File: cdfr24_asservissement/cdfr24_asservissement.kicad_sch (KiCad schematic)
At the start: 0 parts

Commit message: First draft of schematic
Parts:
- added C10: 4.7uF, Capacitor_SMD:C_0805_2012Metric_Pad1.18x1.45mm_HandSolder, symbol Device:C
- added C11: 100uF, Capacitor_SMD:CP_Elec_10x10.5, symbol Device:C_Polarized
- added C14, C15: 10pF, Capacitor_SMD:C_0805_2012Metric_Pad1.18x1.45mm_HandSolder, symbol Device:C
- added C25: 10nF, Capacitor_SMD:C_0805_2012Metric_Pad1.18x1.45mm_HandSolder, symbol Device:C
- added C26: 1uF, Capacitor_SMD:C_0805_2012Metric_Pad1.18x1.45mm_HandSolder, symbol Device:C
- added C27, C28, C29, C30, C32 (x3): 100nF, Capacitor_SMD:C_0805_2012Metric_Pad1.18x1.45mm_HandSolder, symbol Device:C
- added C33: 220uF, Capacitor_SMD:CP_Elec_10x10.5, symbol Device:C_Polarized
- added C7, C8: 470uF, Capacitor_SMD:CP_Elec_10x10.5, symbol Device:C_Polarized
- added D1, D2, D3, D4: LED, LED_SMD:LED_0805_2012Metric_Pad1.15x1.40mm_HandSolder, symbol Device:LED
- added D5: D_Zener, Diode_SMD:D_SOD-123, symbol Device:D_Zener
- added D6: DIODE, B170B:DIOM505270X240, symbol pspice:DIODE
- added J1: Connecteur batterie, TerminalBlockBend:CUI_TBP01R1-508-02BE, symbol Connector:Screw_Terminal_01x02
- added J10: Free Connecteur, Connector_PinHeader_2.54mm:PinHeader_1x08_P2.54mm_Vertical, symbol Connector:Conn_01x08_Male
- added J11, J12: Conn_01x02, Connector_JST:JST_XH_B2B-XH-A_1x02_P2.50mm_Vertical, symbol Connector_Generic:Conn_01x02
- added J13, J6: Connecteur Odométrie, Connector_JST:JST_XH_B4B-XH-A_1x04_P2.50mm_Vertical, symbol Connector_Generic:Conn_01x04
- added J2 (x2): Conn_01x03, TerminalBlockBend:CUI_TBP02R1-381-03BE, symbol Connector_Generic:Conn_01x03
- added J3 (x2): Conn_01x05, Connector_JST:JST_XH_B5B-XH-A_1x05_P2.50mm_Vertical, symbol Connector_Generic:Conn_01x05
- added J4: Connecteur Programmation, Connector_PinHeader_2.54mm:PinHeader_1x04_P2.54mm_Vertical, symbol Connector_Generic:Conn_01x04
- added J5: Conn_01x03, Connector_PinHeader_2.54mm:PinHeader_1x03_P2.54mm_Vertical, symbol Connector_Generic:Conn_01x03
- added J7: Conn_01x03, Connector_JST:JST_XH_B3B-XH-A_1x03_P2.50mm_Vertical, symbol Connector_Generic:Conn_01x03
- added JP1: Jumper_3_Open, Connector_PinHeader_2.54mm:PinHeader_1x03_P2.54mm_Vertical, symbol Jumper:Jumper_3_Open
- added L2: 10uH, IHLP2525CZER100M01:IND_IHLP_2525_CZ-M, symbol Device:L
- added Q13: Q_NMOS_GDS, Package_TO_SOT_SMD:TO-252-2, symbol Device:Q_NMOS_GDS
- added R1, R10, R19, R21, R44, R8: 10k, Resistor_SMD:R_0805_2012Metric_Pad1.20x1.40mm_HandSolder, symbol Device:R
- added R2: 2k4, Resistor_SMD:R_0805_2012Metric_Pad1.20x1.40mm_HandSolder, symbol Device:R
- added R20, R22, R9: 220, Resistor_SMD:R_0805_2012Metric_Pad1.20x1.40mm_HandSolder, symbol Device:R
- added R3: 150, Resistor_SMD:R_0805_2012Metric_Pad1.20x1.40mm_HandSolder, symbol Device:R
- added R4: 3k9, Resistor_SMD:R_0805_2012Metric_Pad1.20x1.40mm_HandSolder, symbol Device:R
- added R42, R43 (x3): 56k, Resistor_SMD:R_0805_2012Metric_Pad1.20x1.40mm_HandSolder, symbol Device:R
- added U1: LM317_SOT-223, Package_TO_SOT_SMD:SOT-223-3_TabPin2, symbol Regulator_Linear:LM317_SOT-223
- added U3: STM32F401RCTx, Package_QFP:LQFP-64_10x10mm_P0.5mm, symbol MCU_ST_STM32F4:STM32F401RCTx
- added U4: LSM6DSL, Package_LGA:LGA-14_3x2.5mm_P0.5mm_LayoutBorder3x4y, symbol Sensor_Motion:LSM6DSL
- added U4: LMR16020PDDA, Package_SO:SOIC-8-1EP_3.9x4.9mm_P1.27mm_EP2.41x3.3mm, symbol LMR16020PDDA:LMR16020PDDA
- added Y1: Crystal_GND24, Crystal:Crystal_SMD_2520-4Pin_2.5x2.0mm, symbol Device:Crystal_GND24
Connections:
- new net: JP1.2 (C), R21.1
- new net: J13.3 (Pin_3), U3.27 (PB1)
- new net: C14.2, R1.1, Y1.3
- new net: R1.2, U3.5 (PH0)
- new net: D4.1 (K), R22.1
- new net: J6.2 (Pin_2), U3.56 (PB4)
- new net: J6.3 (Pin_3), U3.57 (PB5)
- new net: D4.2 (A), U3.50 (PA15)
- new net: C32.2, D6.2 (A), L2.1, U4.8 (SW)
- new net: D5.1 (K), Q13.1 (G), R42.2
- new net: C15.1, R8.1, Y1.1
- new net: R8.2, U3.6 (PH1)
- new net: C32.1, U4.1 (BOOT)
- new net: D3.1 (K), R20.1
- new net: D3.2 (A), U3.45 (PA12)
- new net: J1.2 (Pin_2), Q13.2 (D)
- new net: R2.2, R4.1, U1.1 (ADJ)
- new net: R43.2, R44.1, U4.5 (FB)
- new net: J12.2 (Pin_2), R19.2, U3.52 (PC11)
- new net: D2.1 (K), R9.1
- new net: R21.2, U3.60 (BOOT0)
- new net: C10.1, U3.30 (VCAP1)
- new net: J11.2 (Pin_2), R10.2, U3.53 (PC12)
- new net: J4.4 (Pin_4), U3.7 (NRST)
- new net: D1.1 (K), R3.1
- new net +3.3V: C11.1, C25.1, C26.1, C27.1, C28.1, C29.1, C30.1, C32.1, C32.2, D1.2 (A), J11.1 (Pin_1), J12.1 (Pin_1), JP1.3 (B), R2.1, R43.1, R43.1, U1.2 (VO), U3.1 (VBAT), U3.13 (VREF+), U3.19 (VDD), U3.32 (VDD), U3.48 (VDD), U3.64 (VDD), U4.12 (CS), U4.5 (VDDIO), U4.8 (VDD)
- new net +5V: C33.1, D2.2 (A), J13.4 (Pin_4), J3.1 (Pin_1), J3.1 (Pin_1), J6.4 (Pin_4), L2.2, R43.1, U1.3 (VI)
- new net +BATT: C7.1, C8.1, J1.1 (Pin_1), R42.1, U4.2 (VIN), U4.3 (EN)
- new net BRAKE_L: U3.22 (PA6)
- new net BRAKE_R: U3.36 (PB15)
- new net EN_L: U3.23 (PA7)
- new net EN_R: U3.38 (PC7)
- new net FWD_L: U3.26 (PB0)
- new net FWD_R: U3.34 (PB13)
- new net Free1: J10.1 (Pin_1), U3.62 (PB9)
- new net Free2: J10.2 (Pin_2), U3.2 (PC13)
- new net Free3: J10.3 (Pin_3), U3.3 (PC14)
- new net Free4: J10.4 (Pin_4), U3.4 (PC15)
- new net Free5: J10.5 (Pin_5), U3.8 (PC0)
- new net Free6: J10.6 (Pin_6), U3.9 (PC1)
- new net Free7: J10.7 (Pin_7), U3.10 (PC2)
- new net Free8: J10.8 (Pin_8), U3.11 (PC3)
- new net GND: C10.2, C11.2, C14.1, C15.2, C25.2, C26.2, C27.2, C28.2, C29.2, C30.2, C32.1, C32.2, C33.2, C7.2, C8.2, D5.2 (A), D6.1 (K), J13.1 (Pin_1), J3.5 (Pin_5), J3.5 (Pin_5), J4.1 (Pin_1), J5.3 (Pin_3), J6.1 (Pin_1), J7.3 (Pin_3), JP1.1 (A), Q13.3 (S), R10.1, R19.1, R20.2, R22.2, R3.2, R4.2, R44.2, R9.2, U3.12 (VSSA), U3.18 (VSS), U3.31 (VSS), U3.47 (VSS), U3.63 (VSS), U4.1 (SDO/SA0), U4.2 (SDX), U4.3 (SCX), U4.4 (RT/SYNC), U4.6 (GND), U4.7 (GND), U4.7 (GND), U4.9 (THERMAL_PAD), Y1.2, Y1.4
- new net I2C_CLK: J7.1 (Pin_1), U3.58 (PB6)
- new net I2C_SDA: J7.2 (Pin_2), U3.59 (PB7)
- new net IMU_INT1: U3.41 (PA8), U4.4 (INT1)
- new net IMU_INT2: U3.42 (PA9), U4.9 (INT2)
- new net IMU_SCL: R43.2, U3.29 (PB10), U4.13 (SCL)
- new net IMU_SDA: R43.2, U3.55 (PB3), U4.14 (SDA)
- new net RX: J5.2 (Pin_2), U3.17 (PA3)
- new net SWCLK: J4.2 (Pin_2), U3.49 (PA14)
- new net SWDIO: J4.3 (Pin_3), U3.46 (PA13)
- new net TACHO_L: U3.21 (PA5)
- new net TACHO_R: U3.37 (PC6)
- new net TX: J5.1 (Pin_1), U3.16 (PA2)
- new net left_driver/H1: J3.4 (Pin_4)
- new net left_driver/H2: J3.3 (Pin_3)
- new net left_driver/H3: J3.2 (Pin_2)
- new net left_driver/OUT1: J2.3 (Pin_3)
- new net left_driver/OUT2: J2.2 (Pin_2)
- new net left_driver/OUT3: J2.1 (Pin_1)
- new net odometrie2: J13.2 (Pin_2), U3.54 (PD2)
- new net right_driver/H1: J3.4 (Pin_4)
- new net right_driver/H2: J3.3 (Pin_3)
- new net right_driver/H3: J3.2 (Pin_2)
- new net right_driver/OUT1: J2.3 (Pin_3)
- new net right_driver/OUT2: J2.2 (Pin_2)
- new net right_driver/OUT3: J2.1 (Pin_1)
- no-connect marks 0 -> 15
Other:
- added sheet left_driver (motor_driver.kicad_sch)
- added sheet right_driver (motor_driver.kicad_sch)
- note added: "3,6 v max pour VBATT (alim pour quartz) et 4 pour VDD"
- note added: "A verifier pour 2024 Speed_controle_1 : TIM1_CH2N Speed_controle_2 : TIM1_CH1N Info_vitesse_1 : TIM2 Info_vitesse_2 : TM3 Info_Courant_1 : ADC_IN1 Info_Courant_2 : ADC_IN11"
- note added: "Alimentation"
- note added: "I2C address 1101010b"
- note added: "I2C mode enabled"
- note added: "Speed control pin"
- note added: "TODO: Add the STlink directly"

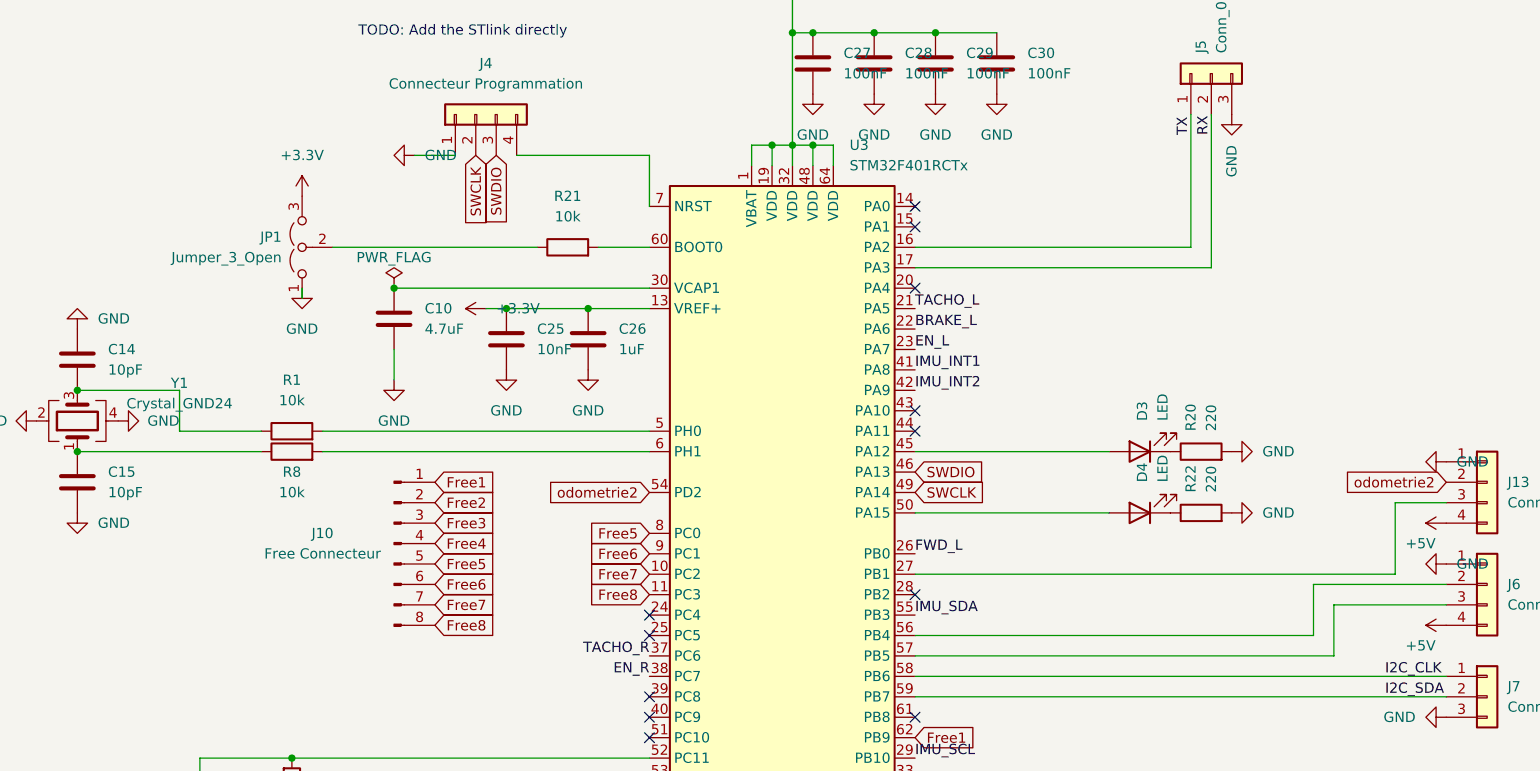
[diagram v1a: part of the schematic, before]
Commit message: change EXTI and boot0 pin connection
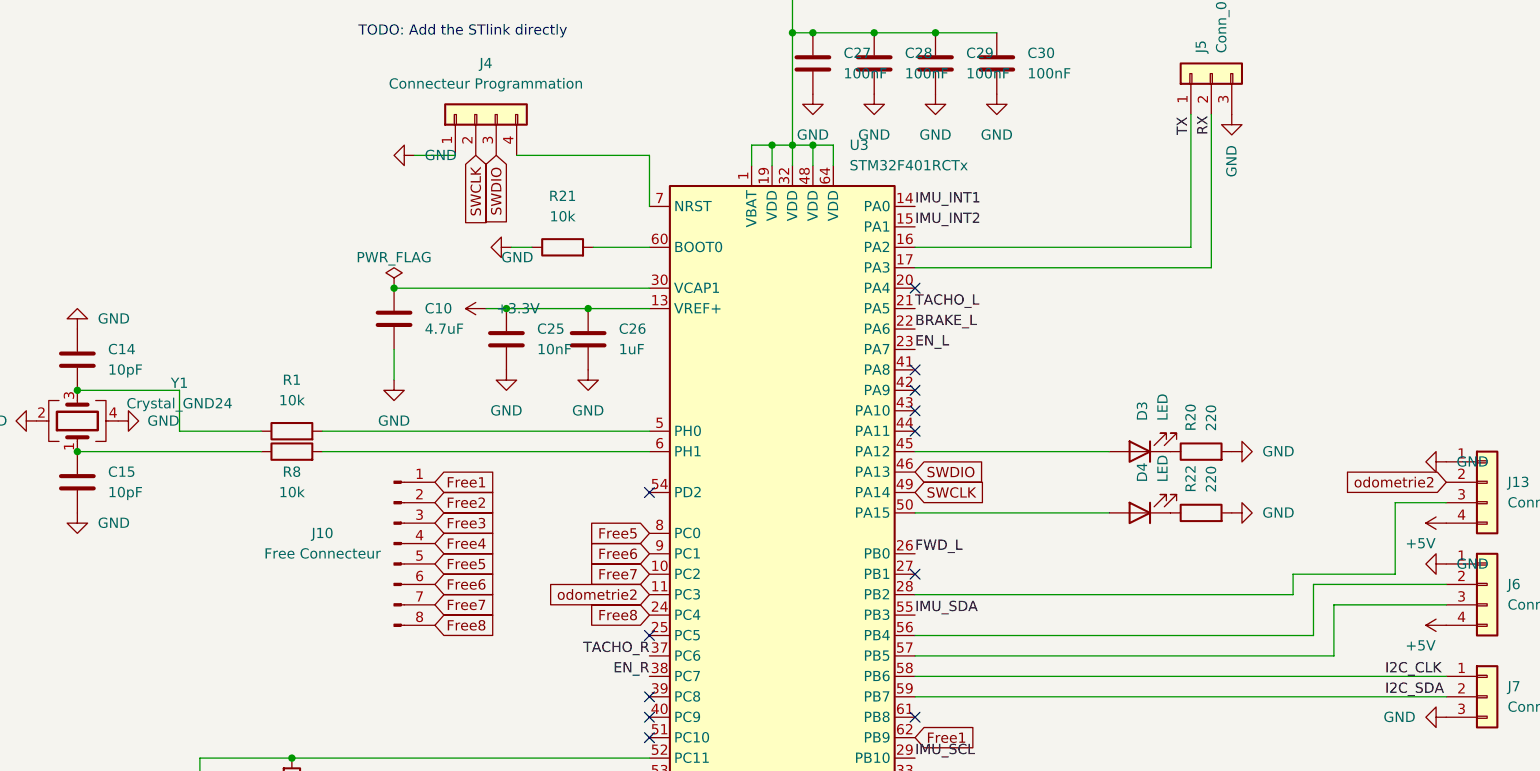
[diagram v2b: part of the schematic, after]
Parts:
- removed JP1: Jumper_3_Open, Connector_PinHeader_2.54mm:PinHeader_1x03_P2.54mm_Vertical, symbol Jumper:Jumper_3_Open
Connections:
- net Free8: now also U3.24 (PC4); no longer U3.11 (PC3)
- net GND: now also R21.1
- net IMU_INT1: now also U3.14 (PA0); no longer U3.41 (PA8)
- net IMU_INT2: now also U3.15 (PA1); no longer U3.42 (PA9)
- net odometrie2: now also U3.11 (PC3); no longer U3.54 (PD2)
- net at J13.3 (Pin_3): now also U3.28 (PB2); no longer U3.27 (PB1)
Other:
- moved on the sheet: R21
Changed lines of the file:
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@@
   (no_connect (at 130.175 307.34))
   (no_connect (at 130.175 304.8))
+  (no_connect (at 163.195 289.56))
   (no_connect (at 130.175 309.88))
-  (no_connect (at 130.175 294.64))
   (no_connect (at 83.185 53.975))
   (no_connect (at 163.195 314.96))
@@
   (no_connect (at 163.195 271.78))
   (no_connect (at 163.195 269.24))
-  (no_connect (at 163.195 292.1))
+  (no_connect (at 130.175 279.4))
   (no_connect (at 163.195 254))
-  (no_connect (at 163.195 243.84))
-  (no_connect (at 163.195 246.38))
+  (no_connect (at 163.195 264.16))
   (no_connect (at 163.195 307.34))
+  (no_connect (at 163.195 266.7))
   (wire (pts (xy 335.026 218.44) (xy 345.567 218.44))
     (stroke (width 0) (type default))
@@
     (stroke (width 0) (type default))
   )
+  (wire (pts (xy 210.185 289.56) (xy 222.885 289.56))
+    (stroke (width 0) (type default))
+  )
   (wire (pts (xy 262.255 56.515) (xy 262.255 61.595))
     (stroke (width 0) (type default))
@@
     (stroke (width 0) (type default))
   )
+  (wire (pts (xy 163.195 292.1) (xy 210.185 292.1))
+    (stroke (width 0) (type default))
+  )
   (wire (pts (xy 146.685 66.675) (xy 159.385 66.675))
     (stroke (width 0) (type default))
@@
     (stroke (width 0) (type default))
   )
-  (wire (pts (xy 123.825 248.92) (xy 130.175 248.92))
+  (wire (pts (xy 123.19 248.92) (xy 130.175 248.92))
     (stroke (width 0) (type default))
   )
@@
     (stroke (width 0) (type default))
   )
-  (wire (pts (xy 116.205 248.92) (xy 90.805 248.92))
-    (stroke (width 0) (type default))
-  )
   (wire (pts (xy 159.385 46.355) (xy 159.385 66.675))
     (stroke (width 0) (type default))
@@
     (stroke (width 0) (type default))
   )
+  (wire (pts (xy 113.03 248.92) (xy 115.57 248.92))
+    (stroke (width 0) (type default))
+  )
   (wire (pts (xy 147.828 128.016) (xy 153.162 128.016))
     (stroke (width 0) (type default))
@@
     (stroke (width 0) (type default))
   )
+  (wire (pts (xy 210.185 292.1) (xy 210.185 289.56))
+    (stroke (width 0) (type default))
+  )
   (wire (pts (xy 150.495 327.66) (xy 150.495 331.47))
     (stroke (width 0) (type default))
@@
     (stroke (width 0) (type default))
   )
-  (wire (pts (xy 86.995 254) (xy 86.995 255.27))
-    (stroke (width 0) (type default))
-  )
   (wire (pts (xy 466.852 216.916) (xy 482.6 216.916))
     (stroke (width 0) (type default))
@@
     (stroke (width 0) (type default))
   )
-  (wire (pts (xy 163.195 289.56) (xy 222.885 289.56))
-    (stroke (width 0) (type default))
-  )
   (wire (pts (xy 127.635 66.675) (xy 146.685 66.675))
     (stroke (width 0) (type default))
@@
     (effects (font (size 1.27 1.27)) (justify left bottom))
   )
-  (label "IMU_INT2" (at 163.195 266.7 0) (fields_autoplaced)
+  (label "IMU_INT2" (at 163.195 246.38 0) (fields_autoplaced)
     (effects (font (size 1.27 1.27)) (justify left bottom))
   )
@@
     (effects (font (size 1.27 1.27)) (justify left bottom))
   )
-  (label "IMU_INT1" (at 163.195 264.16 0) (fields_autoplaced)
+  (label "IMU_INT1" (at 163.195 243.84 0) (fields_autoplaced)
     (effects (font (size 1.27 1.27)) (justify left bottom))
   )
@@
     )
   )
-  (global_label "Free8" (shape input) (at 130.175 292.1 180) (fields_autoplaced)
+  (global_label "Free8" (shape input) (at 130.175 294.64 180) (fields_autoplaced)
     (effects (font (size 1.27 1.27)) (justify right))
-    (property "Intersheetrefs" "${INTERSHEET_REFS}" (at 122.5005 292.0206 0)
+    (property "Intersheetrefs" "${INTERSHEET_REFS}" (at 122.5005 294.5606 0)
       (effects (font (size 1.27 1.27)) (justify right) hide)
     )
@@
     )
   )
-  (global_label "odometrie2" (shape input) (at 130.175 279.4 180) (fields_autoplaced)
+  (global_label "odometrie2" (shape input) (at 130.175 292.1 180) (fields_autoplaced)
     (effects (font (size 1.27 1.27)) (justify right))
-    (property "Intersheetrefs" "${INTERSHEET_REFS}" (at 117.1181 279.3206 0)
+    (property "Intersheetrefs" "${INTERSHEET_REFS}" (at 116.6255 292.1 0)
       (effects (font (size 1.27 1.27)) (justify right) hide)
     )
@@
     )
   )
-  (symbol (lib_id "Jumper:Jumper_3_Open") (at 86.995 248.92 90) (unit 1)
-    (in_bom yes) (on_board yes) (dnp no) (fields_autoplaced)
-    (property "Reference" "JP1" (at 84.455 247.6499 90)
-      (effects (font (size 1.27 1.27)) (justify left))
-    )
-    (property "Value" "Jumper_3_Open" (at 84.455 250.1899 90)
-      (effects (font (size 1.27 1.27)) (justify left))
-    )
-    (property "Footprint" "Connector_PinHeader_2.54mm:PinHeader_1x03_P2.54mm_Vertical" (at 86.995 248.92 0)
-      (effects (font (size 1.27 1.27)) hide)
-    )
-    (property "Datasheet" "~" (at 86.995 248.92 0)
-      (effects (font (size 1.27 1.27)) hide)
-    )
-    (pin "1")
-    (pin "2")
-    (pin "3")
-    (instances
-      (project "Asservissement_CDFR_2023"
-        (path "/aba37299-4f54-471d-ab35-d760532fd54c"
-          (reference "JP1") (unit 1)
-        )
-      )
-      (project "cdfr24_asservissement"
-        (path "/c6b82269-16f5-49e6-8b51-4d12a40a3077"
-          (reference "JP1") (unit 1)
-        )
-      )
-    )
-  )
   (symbol (lib_id "Connector_Generic:Conn_01x04") (at 234.315 278.13 0) (unit 1)
     (in_bom yes) (on_board yes) (dnp no)
@@
     )
   )
-  (symbol (lib_id "Device:R") (at 120.015 248.92 90) (unit 1)
+  (symbol (lib_id "Device:R") (at 119.38 248.92 90) (unit 1)
     (in_bom yes) (on_board yes) (dnp no) (fields_autoplaced)
-    (property "Reference" "R21" (at 120.015 242.57 90)
+    (property "Reference" "R21" (at 119.38 242.57 90)
       (effects (font (size 1.27 1.27)))
     )
-    (property "Value" "10k" (at 120.015 245.11 90)
+    (property "Value" "10k" (at 119.38 245.11 90)
       (effects (font (size 1.27 1.27)))
     )
-    (property "Footprint" "Resistor_SMD:R_0805_2012Metric_Pad1.20x1.40mm_HandSolder" (at 120.015 250.698 90)
+    (property "Footprint" "Resistor_SMD:R_0805_2012Metric_Pad1.20x1.40mm_HandSolder" (at 119.38 250.698 90)
       (effects (font (size 1.27 1.27)) hide)
     )
-    (property "Datasheet" "~" (at 120.015 248.92 0)
+    (property "Datasheet" "~" (at 119.38 248.92 0)
       (effects (font (size 1.27 1.27)) hide)
     )
@@
     )
   )
-  (symbol (lib_id "power:GND") (at 86.995 254 0) (unit 1)
-    (in_bom yes) (on_board yes) (dnp no) (fields_autoplaced)
-    (property "Reference" "#PWR035" (at 86.995 260.35 0)
+  (symbol (lib_id "power:GND") (at 113.03 248.92 270) (unit 1)
+    (in_bom yes) (on_board yes) (dnp no)
+    (property "Reference" "#PWR035" (at 106.68 248.92 0)
       (effects (font (size 1.27 1.27)) hide)
     )
-    (property "Value" "GND" (at 86.995 259.08 0)
-      (effects (font (size 1.27 1.27)))
+    (property "Value" "GND" (at 111.76 250.19 90)
+      (effects (font (size 1.27 1.27)) (justify left))
     )
-    (property "Footprint" "" (at 86.995 254 0)
+    (property "Footprint" "" (at 113.03 248.92 0)
       (effects (font (size 1.27 1.27)) hide)
     )
-    (property "Datasheet" "" (at 86.995 254 0)
+    (property "Datasheet" "" (at 113.03 248.92 0)
       (effects (font (size 1.27 1.27)) hide)
     )
@@
         )
       )
-    )
-  )
-  (symbol (lib_id "power:+3.3V") (at 86.995 242.57 0) (unit 1)
-    (in_bom yes) (on_board yes) (dnp no) (fields_autoplaced)
-    (property "Reference" "#PWR030" (at 86.995 246.38 0)
-      (effects (font (size 1.27 1.27)) hide)
-    )
-    (property "Value" "+3.3V" (at 86.995 237.49 0)
-      (effects (font (size 1.27 1.27)))
-    )
-    (property "Footprint" "" (at 86.995 242.57 0)
-      (effects (font (size 1.27 1.27)) hide)
-    )
-    (property "Datasheet" "" (at 86.995 242.57 0)
-      (effects (font (size 1.27 1.27)) hide)
-    )
-    (pin "1")
-    (instances
-      (project "Asservissement_CDFR_2023"
-        (path "/aba37299-4f54-471d-ab35-d760532fd54c"
-          (reference "#PWR030") (unit 1)
-        )
-      )
-      (project "cdfr24_asservissement"
-        (path "/c6b82269-16f5-49e6-8b51-4d12a40a3077"
-          (reference "#PWR015") (unit 1)
-        )
-      )
